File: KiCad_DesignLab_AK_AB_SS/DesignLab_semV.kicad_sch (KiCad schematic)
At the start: 16 parts, among them U1 ATmega328PB-A, U2 AMS1117-3.3, U3 CC56-12EWA, U5 SDcard_Reader, Y1 Crystal

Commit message: Routed power lines
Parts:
- removed U5: SDcard_Reader, Custom_footprints:SD_Card_Device_custom, symbol Custom_symbols:SDcard_Reader
- added C5, C6, C7: 100n, Capacitor_SMD:C_1210_3225Metric, symbol Device:C
- added J1: Conn_01x04_Pin, Connector_PinHeader_1.00mm:PinHeader_1x04_P1.00mm_Vertical, symbol Connector:Conn_01x04_Pin
- added J2: Barrel_Jack_MountingPin, Connector_BarrelJack:BarrelJack_CUI_PJ-063AH_Horizontal, symbol Connector:Barrel_Jack_MountingPin
- Y1: footprint Crystal:Crystal_HC52-U_Vertical -> Crystal:Crystal_SMD_2016-4Pin_2.0x1.6mm
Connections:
- net 3.3V: now also C6.1
- net GND: now also C5.2, C6.2, C7.2, J2.2
- net VCC: now also C5.1, C7.1, J2.1
- net CS: now reaches U1.14 (PB2)
- net CS: now also J1.4 (Pin_4)
- net MISO: now reaches U1.16 (PB4)
- net MISO: now also J1.3 (Pin_3)
- net MOSI: now reaches U1.15 (PB3)
- net MOSI: now also J1.2 (Pin_2)
- net SCK: now reaches U1.17 (PB5)
- net SCK: now also J1.1 (Pin_1)
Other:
- moved on the sheet: C3, C4

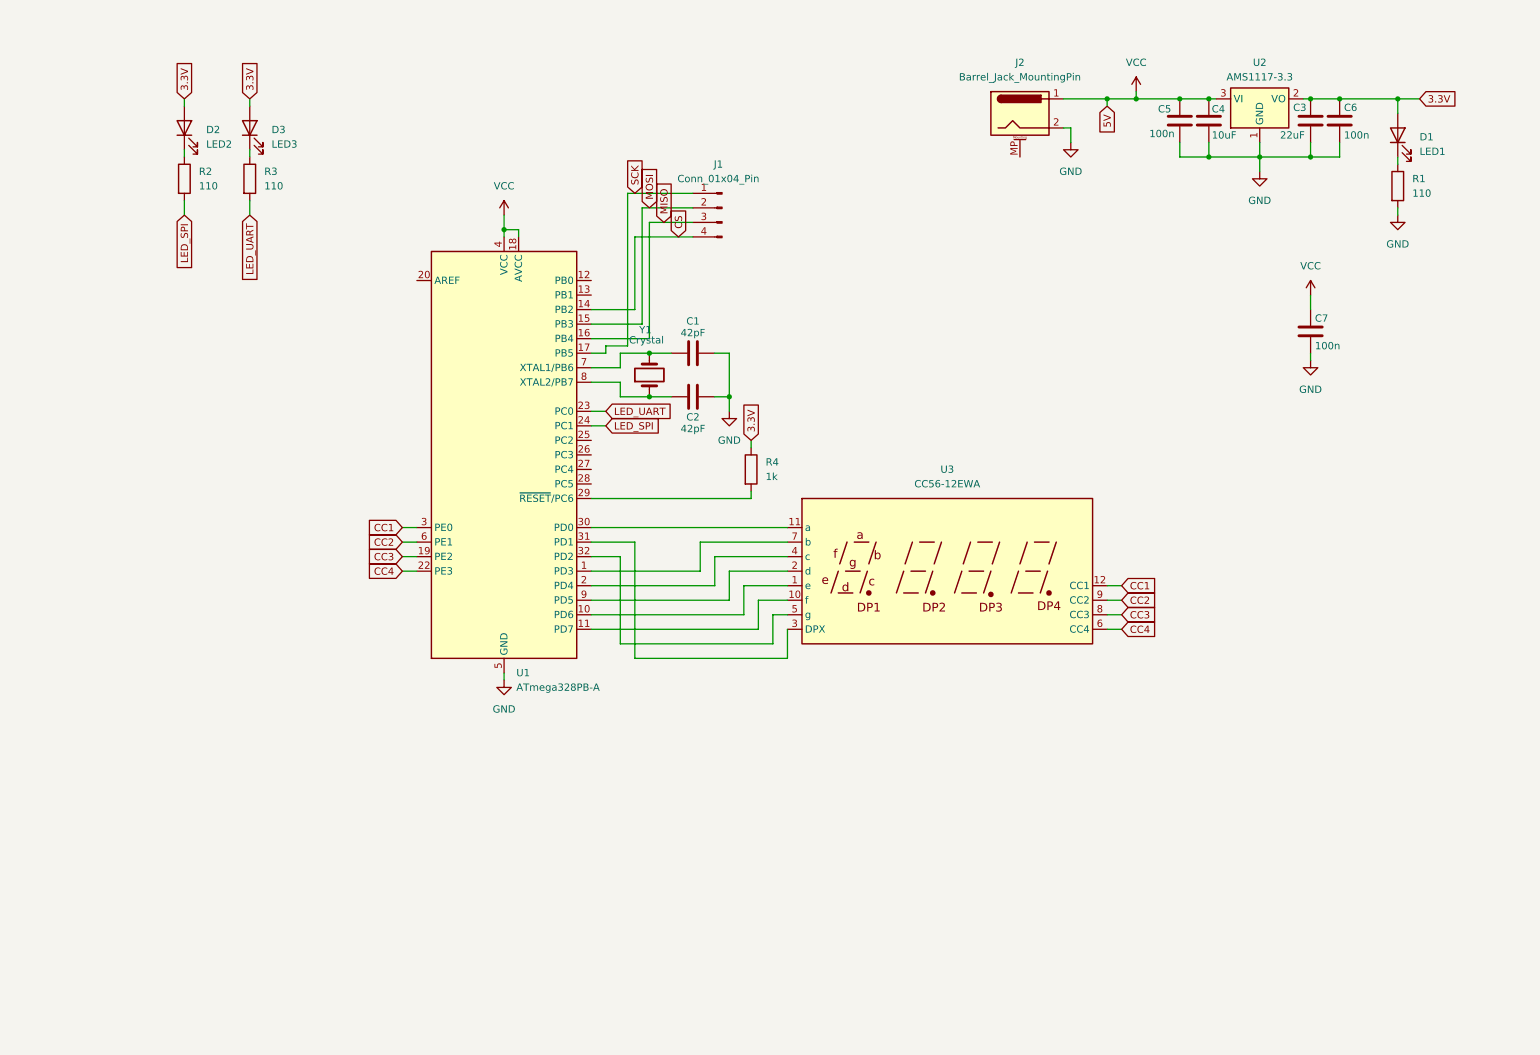
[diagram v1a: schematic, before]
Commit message: Updated the schematic with sensors
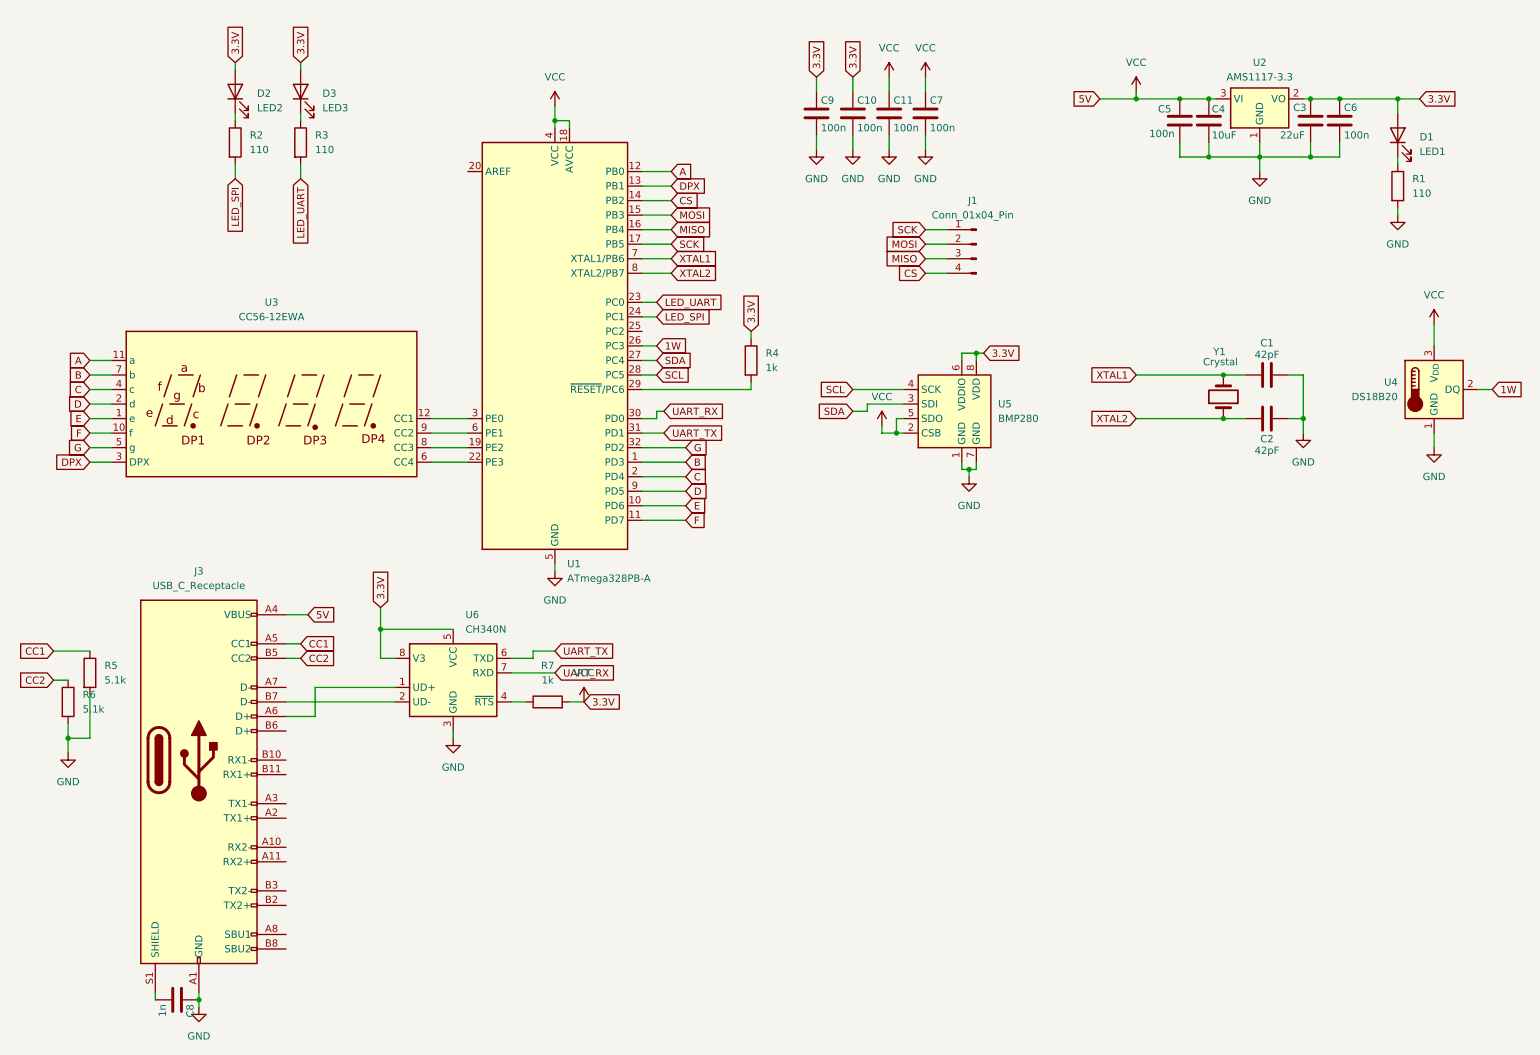
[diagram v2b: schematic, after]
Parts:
- removed J2: Barrel_Jack_MountingPin, Connector_BarrelJack:BarrelJack_CUI_PJ-063AH_Horizontal, symbol Connector:Barrel_Jack_MountingPin
- added C10, C11, C9: 100n, Capacitor_SMD:C_1210_3225Metric, symbol Device:C
- added C8: 1n, Capacitor_SMD:C_1210_3225Metric, symbol Device:C
- added J3: USB_C_Receptacle, Connector_USB:USB_C_Receptacle_Amphenol_12401548E4-2A, symbol Connector:USB_C_Receptacle
- added R5, R6: 5.1k, Resistor_SMD:R_0603_1608Metric, symbol Device:R
- added R7: 1k, Resistor_SMD:R_0603_1608Metric, symbol Device:R
- added U4: DS18B20, Package_TO_SOT_THT:TO-92_Inline, symbol Sensor_Temperature:DS18B20
- added U5: BMP280, Package_LGA:Bosch_LGA-8_2x2.5mm_P0.65mm_ClockwisePinNumbering, symbol Sensor_Pressure:BMP280
- added U6: CH340N, Package_SO:JEITA_SOIC-8_3.9x4.9mm_P1.27mm, symbol Interface_USB:CH340N
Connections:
- net 3.3V is gone; now on net VCC: C3.1, C6.1, D1.2 (A), D2.2 (A), D3.2 (A), R4.1, U2.2 (VO)
- net CC1: now also J3.A5 (CC1), R5.1; no longer U1.3 (PE0), U3.12 (CC1)
- net CC2: now also J3.B5 (CC2), R6.1; no longer U1.6 (PE1), U3.9 (CC2)
- net GND: now also C10.2, C11.2, C8.1, C9.2, J3.A1 (GND), J3.A12 (GND), J3.B1 (GND), J3.B12 (GND), R5.2, R6.2, U4.1 (GND), U5.1 (GND), U5.7 (GND), U6.3 (GND)
- net VCC: now also C10.1, C11.1, C9.1, J3.A4 (VBUS), J3.A9 (VBUS), J3.B4 (VBUS), J3.B9 (VBUS), R7.2, U4.3 (V_{DD}), U5.2 (CSB), U5.5 (SDO), U5.6 (VDDIO), U5.8 (VDD), U6.5 (VCC), U6.8 (V3)
- net XTAL1: now reaches C1.1, U1.7 (XTAL1/PB6), Y1.2
- net E: now reaches U1.10 (PD6), U3.1 (e)
- net F: now reaches U1.11 (PD7), U3.10 (f)
- net A: now reaches U3.11 (a)
- net A: now also U1.12 (PB0); no longer U1.30 (PD0)
- net D: now reaches U1.9 (PD5), U3.2 (d)
- net DPX: now reaches U3.3 (DPX)
- net DPX: now also U1.13 (PB1); no longer U1.31 (PD1)
- net C: now reaches U1.2 (PD4), U3.4 (c)
- net G: now reaches U1.32 (PD2), U3.5 (g)
- net B: now reaches U1.1 (PD3), U3.7 (b)
- net 1W: now reaches U1.26 (PC3)
- net 1W: now also U4.2 (DQ)
- net SDA: now reaches U1.27 (PC4)
- net SDA: now also U5.3 (SDI)
- net SCL: now reaches U1.28 (PC5)
- net SCL: now also U5.4 (SCK)
- net XTAL2: now reaches C2.1, U1.8 (XTAL2/PB7), Y1.1
- net CC3: no longer names the net of U1.19 (PE2), U3.8 (CC3)
- net CC4: no longer names the net of U1.22 (PE3), U3.6 (CC4)
- new net: C8.2, J3.S1 (SHIELD)
- new net: U1.3 (PE0), U3.12 (CC1)
- new net: U1.6 (PE1), U3.9 (CC2)
- new net: J3.A6 (D+), U6.1 (UD+)
- new net: J3.B7 (D-), U6.2 (UD-)
- new net: R7.1, U6.4 (~{RTS})
- new net UART_RX: U1.30 (PD0), U6.7 (RXD)
- new net UART_TX: U1.31 (PD1), U6.6 (TXD)
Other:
- moved on the sheet: C1, C2, C7, D2, D3, J1, R2, R3, R4, U1, U3, Y1

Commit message: Fixed schematic + footprints
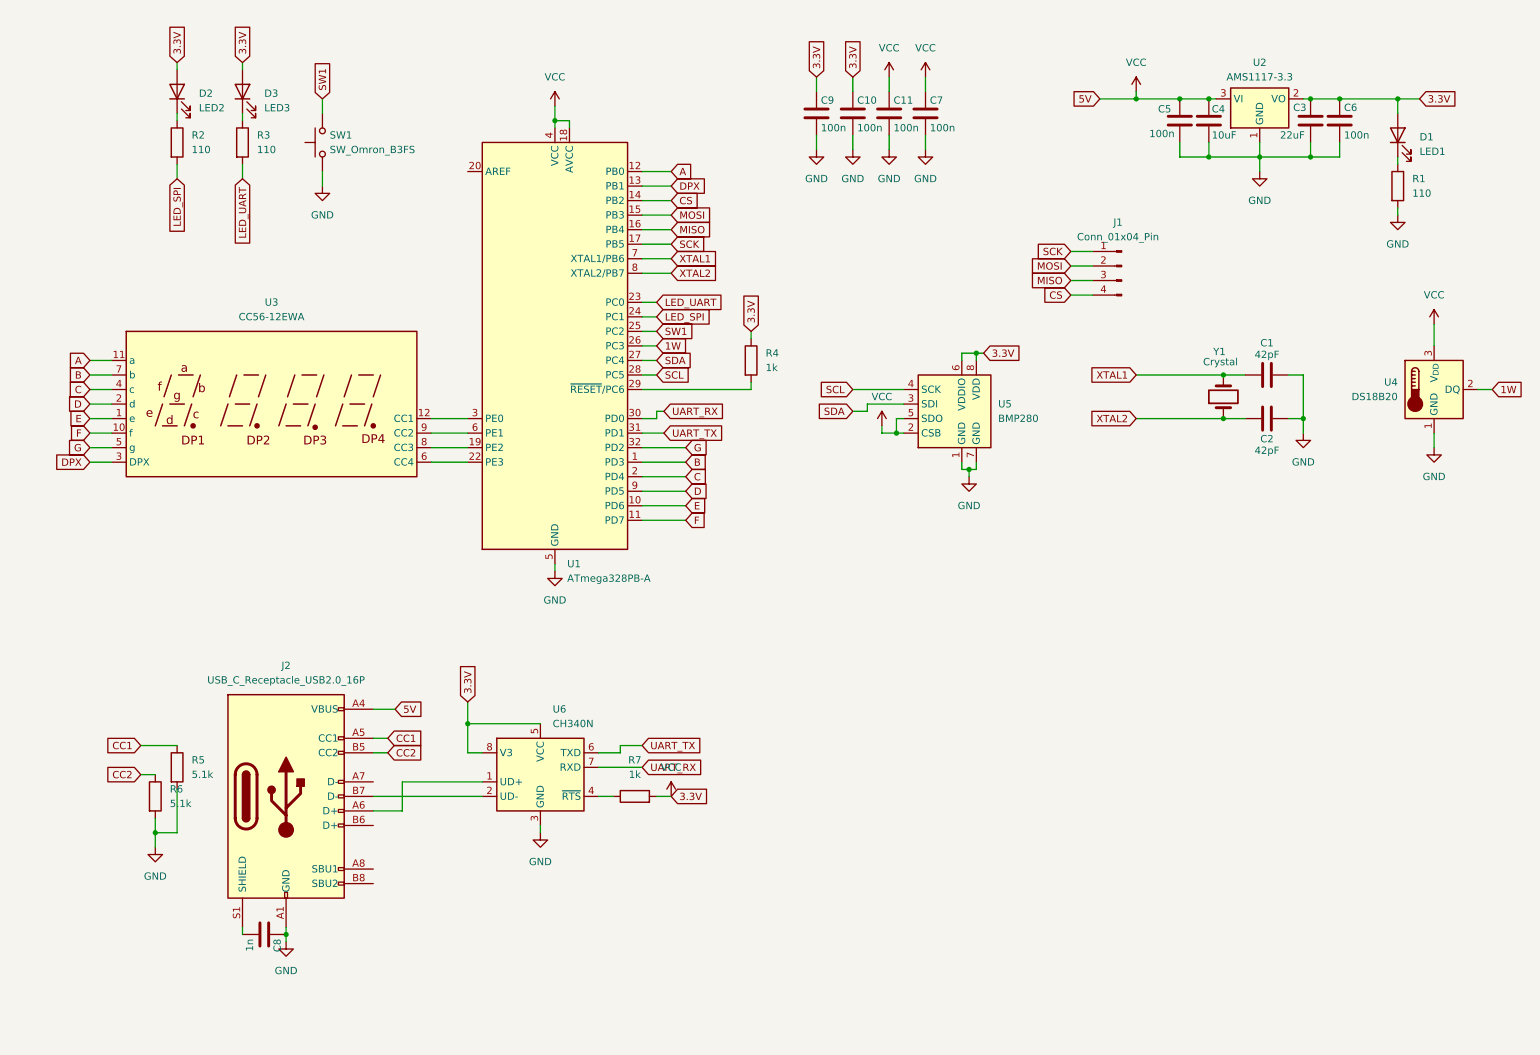
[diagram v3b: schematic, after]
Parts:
- removed J3: USB_C_Receptacle, Connector_USB:USB_C_Receptacle_Amphenol_12401548E4-2A, symbol Connector:USB_C_Receptacle
- added J2: USB_C_Receptacle_USB2.0_16P, Connector_USB:USB_C_Receptacle_HRO_TYPE-C-31-M-12, symbol Connector:USB_C_Receptacle_USB2.0_16P
- added SW1: SW_Omron_B3FS, Button_Switch_SMD:SW_SPST_Omron_B3FS-100xP, symbol Switch:SW_Omron_B3FS
- C1, C10, C11, C2, C3, C4, C5, C6, C7, C8, C9: footprint Capacitor_SMD:C_1210_3225Metric -> Capacitor_SMD:C_0504_1310Metric
- Y1: footprint Crystal:Crystal_SMD_2016-4Pin_2.0x1.6mm -> Crystal:Crystal_SMD_1210-4Pin_1.2x1.0mm
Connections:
- net CC1: now also J2.A5 (CC1)
- net CC2: now also J2.B5 (CC2)
- net GND: now also J2.A1 (GND), J2.A12 (GND), J2.B1 (GND), J2.B12 (GND), SW1.1
- net VCC: now also J2.A4 (VBUS), J2.A9 (VBUS), J2.B4 (VBUS), J2.B9 (VBUS)
- net at C8.2: now also J2.S1 (SHIELD)
- net SW1: now reaches U1.25 (PC2)
- net SW1: now also SW1.2
- net at U6.1 (UD+): now also J2.A6 (D+)
- net at U6.2 (UD-): now also J2.B7 (D-)
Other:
- moved on the sheet: C8, D2, D3, J1, R2, R3, R5, R6, R7, U6

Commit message: Layout before routing
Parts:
- C1, C10, C11, C2, C3, C4, C5, C6, C7, C8, C9: footprint Capacitor_SMD:C_0504_1310Metric -> Capacitor_SMD:C_0603_1608Metric
- J2: footprint Connector_USB:USB_C_Receptacle_HRO_TYPE-C-31-M-12 -> Connector_USB:USB_C_Receptacle_GCT_USB4085
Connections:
- net VCC: no longer C10.1, C3.1, C6.1, C9.1, D1.2 (A), D2.2 (A), D3.2 (A), R4.1, R7.2, U2.2 (VO), U5.6 (VDDIO), U5.8 (VDD), U6.5 (VCC), U6.8 (V3)
- new net 3.3V: C10.1, C3.1, C6.1, C9.1, D1.2 (A), D2.2 (A), D3.2 (A), R4.1, R7.2, U2.2 (VO), U5.6 (VDDIO), U5.8 (VDD), U6.5 (VCC), U6.8 (V3)
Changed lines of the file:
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@@
 		)
 	)
-	(global_label "XTAL1"
+	(global_label "XTAL2"
 		(shape input)
-		(at 132.08 59.69 0)
+		(at 132.08 62.23 0)
 		(fields_autoplaced yes)
 		(effects
@@
 		)
 		(property "Intersheetrefs" "${INTERSHEET_REFS}"
-			(at 140.5685 59.69 0)
+			(at 140.5685 62.23 0)
 			(effects
 				(font
@@
 		)
 	)
-	(global_label "XTAL2"
+	(global_label "XTAL1"
 		(shape input)
-		(at 132.08 62.23 0)
+		(at 132.08 59.69 0)
 		(fields_autoplaced yes)
 		(effects
@@
 		)
 		(property "Intersheetrefs" "${INTERSHEET_REFS}"
-			(at 140.5685 62.23 0)
+			(at 140.5685 59.69 0)
 			(effects
 				(font
@@
 			)
 		)
-		(property "Footprint" "Capacitor_SMD:C_0504_1310Metric"
+		(property "Footprint" "Capacitor_SMD:C_0603_1608Metric"
 			(at 57.15 178.7652 0)
 			(effects
@@
 			)
 		)
-		(property "Footprint" "Capacitor_SMD:C_0504_1310Metric"
+		(property "Footprint" "Capacitor_SMD:C_0603_1608Metric"
 			(at 240.03 79.0448 0)
 			(effects
@@
 	)
 	(symbol
-		(lib_id "power:VCC")
-		(at 132.08 153.67 0)
-		(unit 1)
-		(exclude_from_sim no)
-		(in_bom yes)
-		(on_board yes)
-		(dnp no)
-		(fields_autoplaced yes)
-		(property "Reference" "#PWR019"
-			(at 132.08 157.48 0)
-			(effects
-				(font
-					(size 1.27 1.27)
-				)
-				(hide yes)
-			)
-		)
-		(property "Value" "VCC"
-			(at 132.08 148.59 0)
-			(effects
-				(font
-					(size 1.27 1.27)
-				)
-			)
-		)
-		(property "Footprint" ""
-			(at 132.08 153.67 0)
-			(effects
-				(font
-					(size 1.27 1.27)
-				)
-				(hide yes)
-			)
-		)
-		(property "Datasheet" ""
-			(at 132.08 153.67 0)
-			(effects
-				(font
-					(size 1.27 1.27)
-				)
-				(hide yes)
-			)
-		)
-		(property "Description" "Power symbol creates a global label with name \"VCC\""
-			(at 132.08 153.67 0)
-			(effects
-				(font
-					(size 1.27 1.27)
-				)
-				(hide yes)
-			)
-		)
-		(pin "1"
-		)
-		(instances
-			(project "DesignLab_semV"
-				(path "/66104a27-11ea-4d6a-b2bb-762e8524b9a1"
-					(reference "#PWR019")
-					(unit 1)
-				)
-			)
-		)
-	)
-	(symbol
 		(lib_id "power:GND")
 		(at 170.18 40.64 0)
@@
 			)
 		)
-		(property "Footprint" "Capacitor_SMD:C_0504_1310Metric"
+		(property "Footprint" "Capacitor_SMD:C_0603_1608Metric"
 			(at 227.0252 39.37 0)
 			(effects
@@
 			)
 		)
-		(property "Footprint" "Capacitor_SMD:C_0504_1310Metric"
+		(property "Footprint" "Capacitor_SMD:C_0603_1608Metric"
 			(at 221.9452 39.37 0)
 			(effects
@@
 			)
 		)
-		(property "Footprint" "Capacitor_SMD:C_0504_1310Metric"
+		(property "Footprint" "Capacitor_SMD:C_0603_1608Metric"
 			(at 249.8852 39.37 0)
 			(effects
@@
 			)
 		)
-		(property "Footprint" "Capacitor_SMD:C_0504_1310Metric"
+		(property "Footprint" "Capacitor_SMD:C_0603_1608Metric"
 			(at 244.8052 39.37 0)
 			(effects
@@
 			)
 		)
-		(property "Footprint" "Capacitor_SMD:C_0504_1310Metric"
+		(property "Footprint" "Capacitor_SMD:C_0603_1608Metric"
 			(at 177.4952 38.1 0)
 			(effects
@@
 			)
 		)
-		(property "Footprint" "Connector_USB:USB_C_Receptacle_HRO_TYPE-C-31-M-12"
+		(property "Footprint" "Connector_USB:USB_C_Receptacle_GCT_USB4085"
 			(at 68.58 153.67 0)
 			(effects
@@
 			)
 		)
-		(property "Footprint" "Capacitor_SMD:C_0504_1310Metric"
+		(property "Footprint" "Capacitor_SMD:C_0603_1608Metric"
 			(at 164.7952 38.1 0)
 			(effects
@@
 			)
 		)
-		(property "Footprint" "Capacitor_SMD:C_0504_1310Metric"
+		(property "Footprint" "Capacitor_SMD:C_0603_1608Metric"
 			(at 171.1452 38.1 0)
 			(effects
@@
 			)
 		)
-		(property "Footprint" "Capacitor_SMD:C_0504_1310Metric"
+		(property "Footprint" "Capacitor_SMD:C_0603_1608Metric"
 			(at 240.03 86.6648 0)
 			(effects
@@
 			)
 		)
-		(property "Footprint" "Capacitor_SMD:C_0504_1310Metric"
+		(property "Footprint" "Capacitor_SMD:C_0603_1608Metric"
 			(at 158.4452 38.1 0)
 			(effects

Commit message: Completed PCB v2.0
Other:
- company: (none) -> AGH University of Science and Technology
- title: (none) -> Design Lab EiT - semestr V
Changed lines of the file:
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@@
 	(generator_version "9.0")
 	(paper "A4")
+	(title_block
+		(title "Design Lab EiT - semestr V")
+		(date "2025-12-02")
+		(rev "2.0")
+		(company "AGH University of Science and Technology")
+		(comment 1 "Adrian Bik")
+		(comment 2 "Sebastian Skowron")
+		(comment 3 "Artur Korneluk")
+	)
 	(junction
 		(at 248.92 31.75)
